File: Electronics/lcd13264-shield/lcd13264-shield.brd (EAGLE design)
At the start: 96.6 x 54.6 mm, 30 parts, among them J1 MICRO-SDCARD-CONNECTOR-330006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, J2 ARDUINO_R3_SHIELDUNO_R3_SHIEL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, Q1 PNP-500mA, X1 FH12-12S-1S, X2 FH12-12S-1S

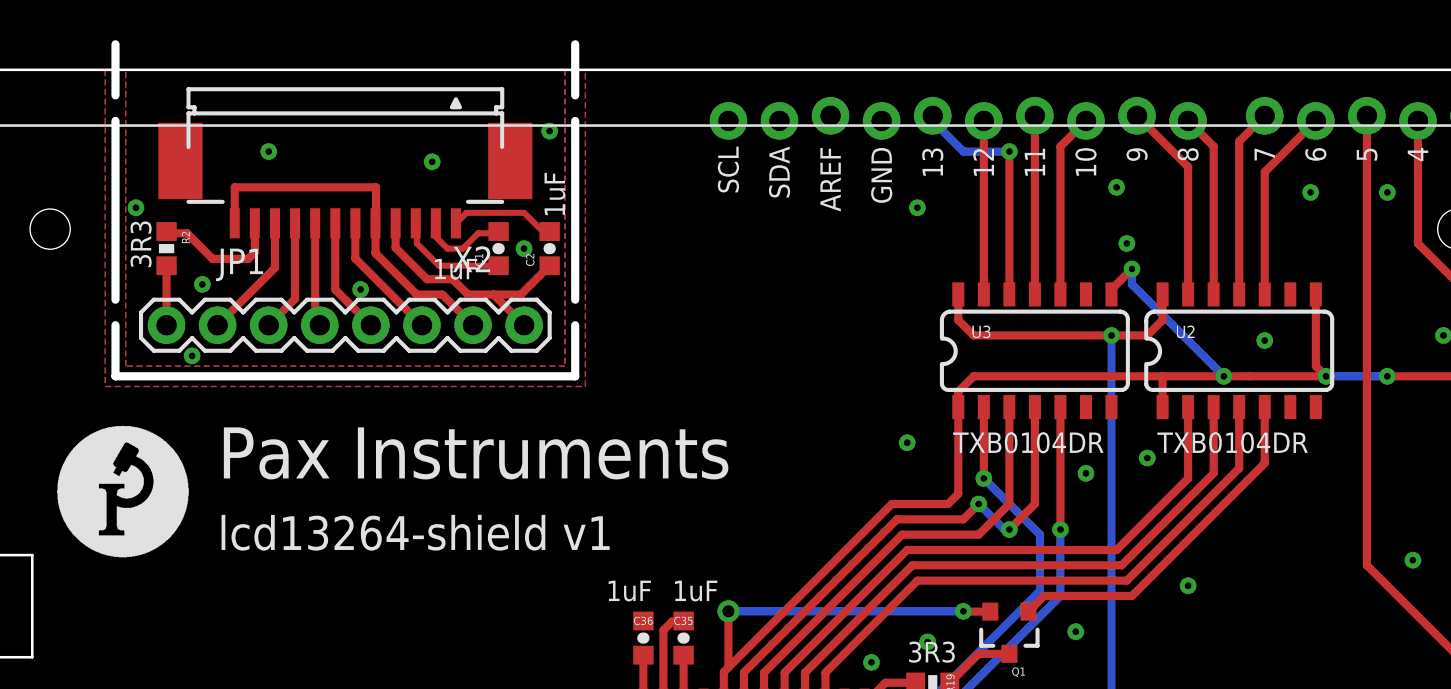
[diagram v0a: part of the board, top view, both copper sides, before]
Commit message: Added bypass caps to level shifter. This closes #1.
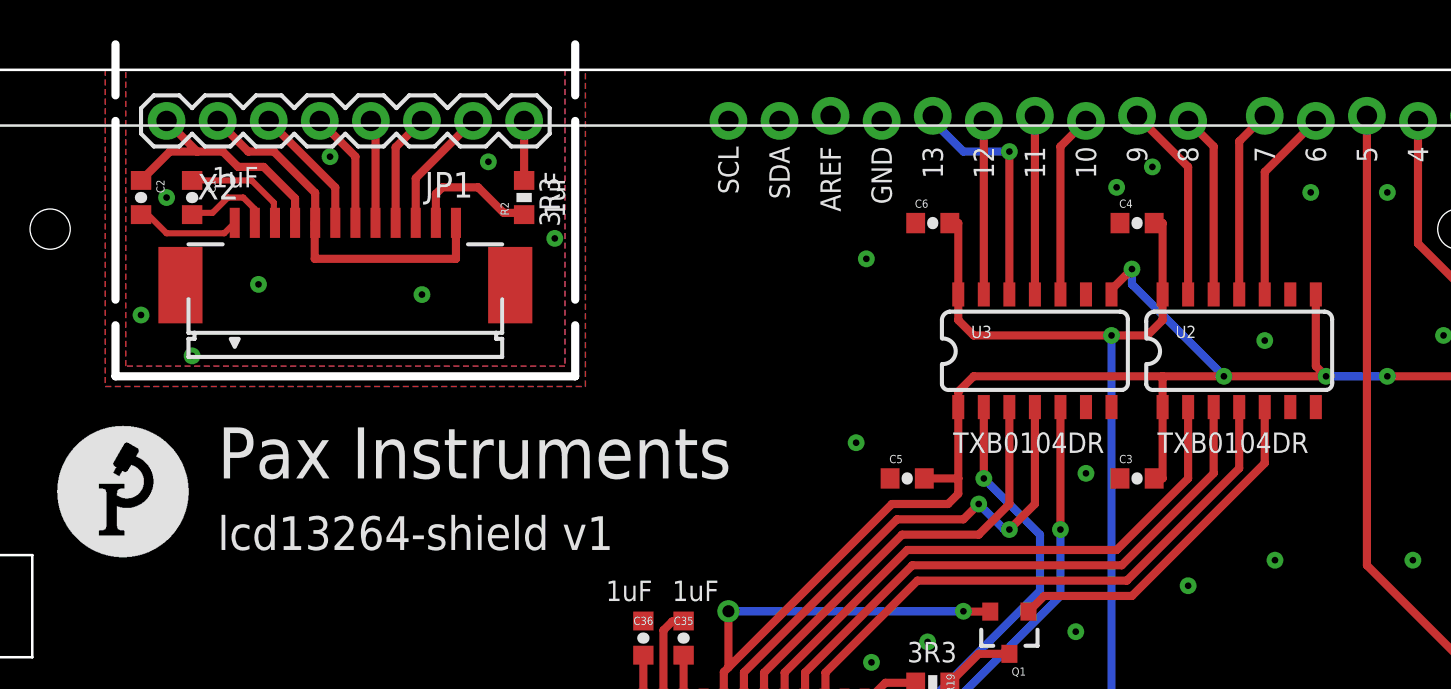
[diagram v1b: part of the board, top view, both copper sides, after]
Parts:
- added C3, C4, C5, C6: 100nF, PaxInstrument-T400:SPARKFUN-CAPACITORS_0603-CAP
- C21: value 0.1uF -> 100nF
- moved C2 20.5 mm to (17.8, 47.0), turned to 270 degrees
- moved JP1 20.5 mm to (36.8, 50.8), turned to 180 degrees
- moved R2 18.0 mm to (36.8, 47.0), turned to 90 degrees
- moved C1 15.5 mm to (20.3, 47.0), turned to 270 degrees
- moved X2 4.57 mm to (27.9, 43.4), turned to 0 degrees
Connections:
- net 3.3V: now also C3.2, C5.2
- net 5V: now also C4.2, C6.2
- net GND: now also C3.1, C4.1, C5.1, C6.1
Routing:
- net 5V: track 51.2 -> 59.1 mm
- net 3.3V: track 237.9 -> 243.6 mm

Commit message: Aupdated shield. Not sure what.
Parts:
- added SJ1, SJ2: JUMPER-PAD-2-NC_BY_PASTE, SparkFun-Passives:PAD-JUMPER-2-NC_BY_PASTE_YES_SILK
- added SJ3: JUMPER-PTH-2-NC, SparkFun-Passives:PTH-JUMPER-NC_BOTTOM_NO_SILK
- moved C6 2.84 mm to (55.9, 43.2)
- moved C4 1.27 mm to (67.3, 44.5)
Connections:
- net N$16 renamed D3
- net N$36 renamed AREF
- removed net N$45: C2.1, JP1.8, X2.4
- net GND: now also C2.1, JP1.8, X2.4
- net SCL: now also SJ2.1, SJ2.2
- net SDA: now also SJ1.1, SJ1.2
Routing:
- net N$45: track 12.6 -> 0.00 mm
- net GND: track 0.00 -> 12.6 mm
- net LCD_BL_5V: track 9.68 -> 0.00 mm
- net LCD_CS_5V: track 9.41 -> 0.00 mm
- net SCK_5V: track 11.8 -> 16.3 mm, vias 1 -> 2
- net AREF: track 0.00 -> 4.32 mm, vias 0 -> 1
- net SDA: track 0.00 -> 3.25 mm, vias 0 -> 1
- net SCL: track 0.00 -> 3.25 mm, vias 0 -> 1
- net 5V: track 59.1 -> 56.6 mm
- net 3.3V: track 243.6 -> 242.7 mm
- net LCD_A0_5V: track 9.94 -> 10.2 mm, vias 0 -> 1
- net SW_B: vias 0 -> 1
- net SW_A: vias 0 -> 1
- net SD_CS_5V: vias 0 -> 1
- net MOSI_5V: vias 0 -> 1
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
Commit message: Close to done. Need to review.
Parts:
- removed J2: ARDUINO_R3_SHIELDUNO_R3_SHIELD_LOCK, SparkFun-Boards:UNO_R3_SHIELD_LOCK
- added J3: ARDUINO_R3_SHIELDUNO_R3_SHIELD_NOLABELS_LOCK, SparkFun-Boards:UNO_R3_SHIELD_NOLABELS_LOCK
- added SJ10, SJ11, SJ12, SJ13, SJ14, SJ19, SJ20, SJ21, SJ22, SJ23, SJ24, SJ25, SJ26, SJ4, SJ5, SJ6, SJ7, SJ8, SJ9: JUMPER-PAD-2-NC_BY_PASTE, SparkFun-Passives:PAD-JUMPER-2-NC_BY_PASTE_YES_SILK
- C1, C2, C21, C3, C35, C36, C4, C5, C6: device PaxInstrument-T400:SPARKFUN-CAPACITORS_0603-CAP -> PaxInstrument-T400:SPARKFUN-CAPACITORS_1206
- R1, R11, R12, R15, R16, R19, R2, R8: device PaxInstrument-T400:SPARKFUN-RESISTORS_0603-RES -> PaxInstrument-T400:SPARKFUN-RESISTORS_1206
- SJ3: value JUMPER-PTH-2-NC -> JUMPER-PAD-2-NC_BY_PASTE; device SparkFun-Passives:PTH-JUMPER-NC_BOTTOM_NO_SILK -> SparkFun-Passives:PAD-JUMPER-2-NC_BY_PASTE_YES_SILK
- moved SJ3 38.4 mm to (81.3, 40.4), turned to 270 degrees
- moved C5 37.1 mm to (41.1, 67.1)
- moved U$1 34.7 mm to (18.5, 63.2)
- moved U$6 34.5 mm to (31.6, 62.0)
- moved C6 25.9 mm to (47.2, 67.6)
- moved C4 23.5 mm to (61.7, 67.3)
- moved R1 21.3 mm to (17.8, 22.9)
- moved U3 17.0 mm to (47.0, 31.8)
- moved U2 14.8 mm to (59.7, 31.8)
- moved R15 14.4 mm to (17.8, 33.0)
- moved R12 14.3 mm to (80.0, 22.9)
- moved R16 13.9 mm to (17.8, 27.9)
- moved R11 13.4 mm to (80.0, 27.9)
- moved R8 13.2 mm to (80.0, 33.0)
- moved C3 12.5 mm to (72.4, 21.6)
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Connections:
- removed net LCD_A0_5V: J2.D9, U2.13
- removed net LCD_BL_5V: J2.D6, U2.10
- removed net LCD_CS_5V: J2.D7, U2.11
- removed net LCD_RST_5V: J2.D8, U2.12
- removed net MISO_5V: J2.D12, U3.13
- removed net MOSI_5V: J2.D11, U3.11
- removed net N$1: J2.IOREF
- removed net N$17: J2.D2
- removed net N$20: J2.TX
- removed net N$25: J2.RX
- removed net N$31: J2.A4
- removed net N$33: J2.A5
- removed net N$34: J2.RES
- removed net N$35: J2.VIN
- removed net SCK_5V: J2.D13, U3.12
- removed net SD_CS_5V: J2.D10, U3.10
- removed net SW_A: J2.D4, R8.2, S3.3
- removed net SW_B: J2.D5, R11.2, S2.3
- removed net SW_C: J2.A3, R12.2, S1.3
- removed net SW_D: J2.A2, R15.2, S4.3
- removed net SW_E: J2.A1, R16.2, S5.3
- removed net SW_F: J2.A0, R1.2, S6.3
- new net A0: J3.A0, R1.2, S6.3, SJ10.1, SJ10.2
- new net A1: J3.A1, R16.2, S5.3, SJ7.1, SJ7.2
- new net A2: J3.A2, R15.2, S4.3, SJ11.1, SJ11.2
- new net A3: J3.A3, R12.2, S1.3, SJ12.1, SJ12.2
- new net A4: J3.A4, SJ13.1, SJ13.2
- new net A5: J3.A5, SJ14.1, SJ14.2
- new net D0: J3.RX, SJ8.1, SJ8.2
- new net D1: J3.TX, SJ9.1, SJ9.2
- new net D10: J3.D10, SJ23.1, SJ23.2, U3.13
- new net D11(MOSI): J3.D11, SJ24.1, SJ24.2, U3.11
- new net D12(MISO): J3.D12, SJ25.1, SJ25.2, U3.12
- new net D13(SCK): J3.D13, SJ26.1, SJ26.2, U3.10
- new net D2: J3.D2, SJ3.1, SJ3.2
- new net D4: J3.D4, R8.2, S3.3, SJ5.1, SJ5.2
- new net D5: J3.D5, R11.2, S2.3, SJ6.1, SJ6.2
- new net D6: J3.D6, SJ19.1, SJ19.2, U2.10
- new net D7: J3.D7, SJ20.1, SJ20.2, U2.11
- new net D8: J3.D8, SJ21.1, SJ21.2, U2.12
- new net D9: J3.D9, SJ22.1, SJ22.2, U2.13
- new net IOREF: J3.IOREF
- new net RESET: J3.RES
- new net VIN: J3.VIN
- net 3.3V: now also J3.3.3V; no longer J2.3.3V
- net 5V: now also J3.5V; no longer J2.5V
- net AREF: now also J3.AREF; no longer J2.AREF
- net D3: now also J3.D3, SJ4.1, SJ4.2; no longer J2.D3
- net GND: now also J3.GND@0, J3.GND@1, J3.GND@2; no longer J2.GND@0, J2.GND@1, J2.GND@2
- net MISO_3V3: now also U3.3; no longer U3.2
- net SCK_3V3: now also U3.5; no longer U3.3
- net SCL: now also J3.SCL; no longer J2.SCL
- net SDA: now also J3.SDA; no longer J2.SDA
- net SD_CS_3V3: now also U3.2; no longer U3.5
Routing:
- net 3.3V: track 242.7 -> 0.00 mm, vias 10 -> 0
- net SW_D: track 108.5 -> 0.00 mm
- net SW_E: track 96.6 -> 0.00 mm
- net SW_F: track 84.5 -> 0.00 mm
- net SCK_3V3: track 59.0 -> 0.00 mm
- net MISO_3V3: track 58.5 -> 0.00 mm, vias 2 -> 0
- net MOSI_3V3: track 58.2 -> 0.00 mm, vias 2 -> 0
- net 5V: track 56.6 -> 0.00 mm, vias 1 -> 0
- net SD_CS_3V3: track 53.1 -> 0.00 mm, vias 2 -> 0
- net SW_B: track 38.9 -> 0.00 mm, vias 1 -> 0
- net LCD_CS_3V3: track 29.4 -> 0.00 mm
- net LCD_RST_3V3: track 29.3 -> 0.00 mm
- net LCD_A0_3V3: track 29.2 -> 0.00 mm
- net SW_A: track 19.5 -> 0.00 mm, vias 1 -> 0
- net N$57: track 17.6 -> 0.00 mm
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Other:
- board size 96.6 x 54.6 mm -> 96.5 x 54.6 mm
- board text added: "0"
- board text added: "1"
- board text added: "10"
- board text added: "11"
- board text added: "12"
- board text added: "13"
- board text added: "2"
- board text added: "3"
- board text added: "3.3V"
- board text added: "4"
- board text added: "5"
- board text added: "5V"
- board text added: "6"
- board text added: "7"
- board text added: "8"
- board text added: "9"
- board text added: "A0"
- board text added: "A1"
- board text added: "A2"
- board text added: "A3"
- board text added: "A4"
- board text added: "A5"
- board text added: "AREF"
- board text added: "GND"
- board text added: "IOREF"
- board text added: "Pin Map SD_CS 10 SW_A 4 SW_B 5 SW_C A3 SW_D A2 SW_E A1 SW_F A0 MOSI 11 MISO 12 LCD_A0 A1 LCD_RST A2 LCD_CS A3 LCD_BL 6 SCL 13"
- board text added: "RESET"
- board text added: "SW_F"
- board text added: "VIN"
- board text removed: "A"
- board text removed: "B"
- board text removed: "C"
- board text removed: "D"
- board text removed: "E"
- board text removed: "F"
- board text removed: "LCD_BL"
- board text removed: "MISO"
- board text removed: "MOSI"
- board text removed: "SCK"
- board text removed: "SD_CS"
- board text removed: "SW_E"
- board text removed: "WS_3v3"
- board text removed: "WS_LIGHT"
- board text removed: "WS_RAIN"
- board text removed: "WS_WDIR"
- board text removed: "WS_WSPEED"

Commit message: This version is done. CAM next...
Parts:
- moved U$6 58.4 mm to (49.5, 6.35)
- moved C5 38.5 mm to (34.3, 29.2)
- moved C6 36.9 mm to (34.3, 33.0)
- moved U$1 36.8 mm to (0.76, 31.0)
- moved C4 35.7 mm to (64.8, 31.8), turned to 180 degrees
- moved C35 10.2 mm to (34.3, 17.8)
- moved C3 9.92 mm to (64.8, 27.9), turned to 180 degrees
- moved Q1 6.48 mm to (62.2, 21.6), turned to 0 degrees
- moved R19 6.35 mm to (62.2, 16.5)
- moved U2 5.57 mm to (54.6, 29.5)
- moved C21 3.81 mm to (19.1, 17.8), turned to 180 degrees
- moved U3 3.42 mm to (44.5, 29.5)
- moved C36 1.80 mm to (34.3, 21.6)
- turned R1 to 180 degrees
- turned R11 to 0 degrees
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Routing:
- net 3.3V: track 0.00 -> 168.5 mm, vias 0 -> 4
- net A2: track 9.35 -> 133.5 mm, vias 2 -> 3
- net A1: track 9.09 -> 114.8 mm, vias 2 -> 3
- net A0: track 9.35 -> 98.1 mm, vias 2 -> 3
- net 5V: track 0.00 -> 75.0 mm, vias 0 -> 4
- net SCK_3V3: track 0.00 -> 43.8 mm, vias 0 -> 2
- net MOSI_3V3: track 0.00 -> 38.3 mm
- net MISO_3V3: track 0.00 -> 33.2 mm
- net D10: track 8.58 -> 40.1 mm, vias 2 -> 3
- net D5: track 8.84 -> 40.3 mm
- net SD_CS_3V3: track 0.00 -> 27.2 mm, vias 0 -> 2
- net A3: track 11.6 -> 38.0 mm
- net D11(MOSI): track 8.84 -> 30.5 mm, vias 2 -> 3
- net D4: track 8.58 -> 30.2 mm
- net D6: track 8.58 -> 28.5 mm
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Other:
- board text added: "Pin Map SD_CS 10 SW_A 4 SW_B 5 SW_C A3 SW_D A2 SW_E A1 SW_F A0 MOSI 11 MISO 12 SCK 13 LCD_A0 9 LCD_RST 8 LCD_CS 7 LCD_BL 6"
- board text added: "SW_E"
- board text removed: "Pin Map SD_CS 10 SW_A 4 SW_B 5 SW_C A3 SW_D A2 SW_E A1 SW_F A0 MOSI 11 MISO 12 LCD_A0 A1 LCD_RST A2 LCD_CS A3 LCD_BL 6 SCL 13"

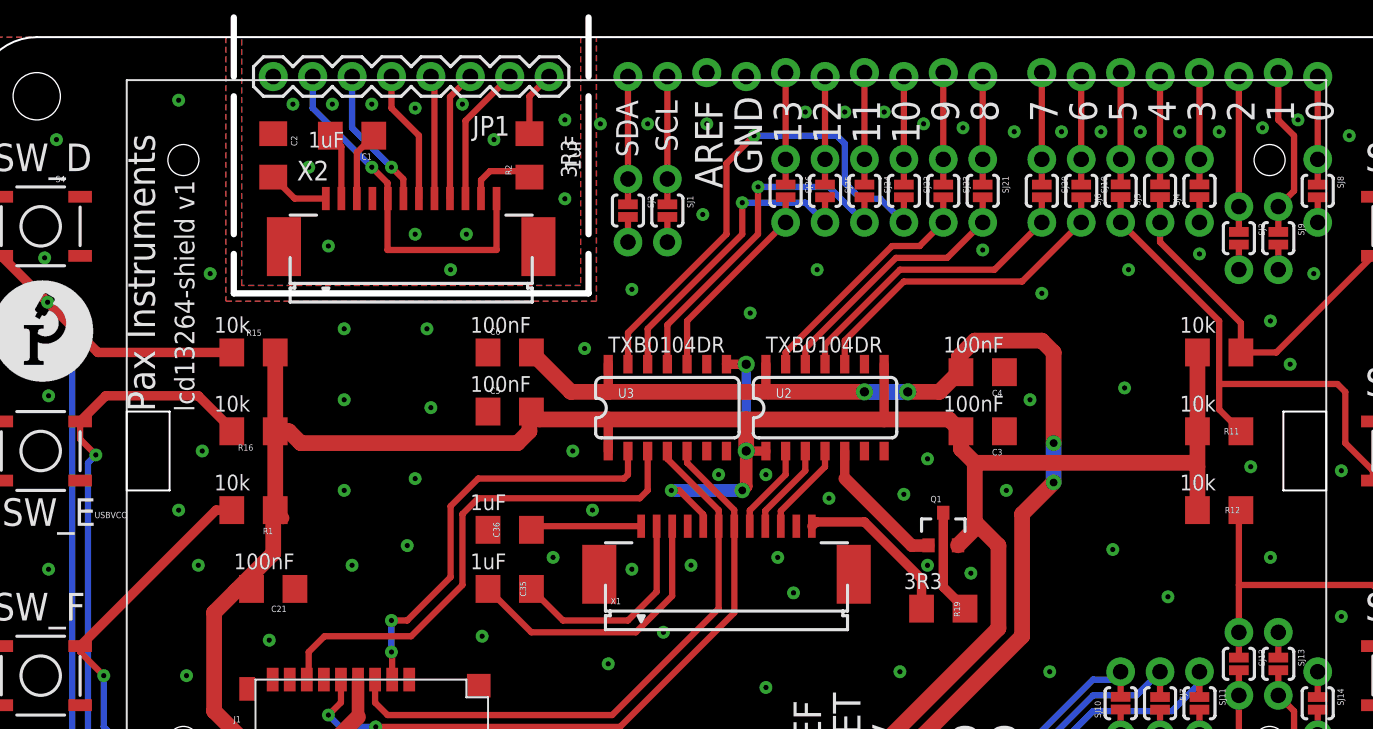
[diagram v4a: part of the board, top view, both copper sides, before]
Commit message: Changed all passives to 0805 and updated traces. Passes DRC.
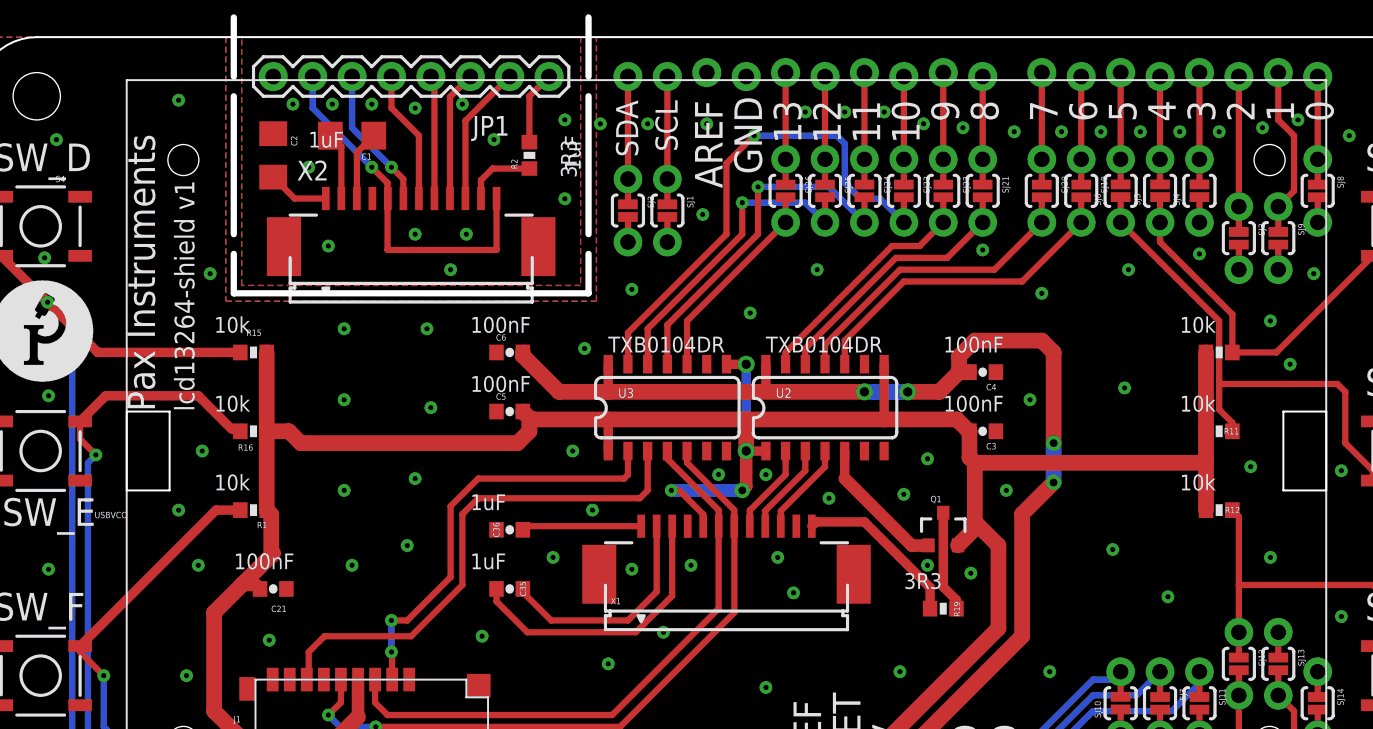
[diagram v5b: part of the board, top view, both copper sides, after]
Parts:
- C21, C3, C35, C36, C4, C5, C6: device PaxInstrument-T400:SPARKFUN-CAPACITORS_1206 -> PaxInstrument-T400:SPARKFUN-CAPACITORS_0603-CAP
- R1, R11, R12, R15, R16, R19, R2, R8: device PaxInstrument-T400:SPARKFUN-RESISTORS_1206 -> PaxInstrument-T400:SPARKFUN-RESISTORS_0603-RES
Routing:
- net 3.3V: track 168.5 -> 169.8 mm
- net 5V: track 75.0 -> 76.2 mm
- net N$38: track 13.9 -> 14.6 mm
- net A0: track 98.1 -> 98.7 mm
- net N$51: track 4.21 -> 4.76 mm
- net N$39: track 7.17 -> 7.72 mm
- net A2: track 133.5 -> 134.0 mm
